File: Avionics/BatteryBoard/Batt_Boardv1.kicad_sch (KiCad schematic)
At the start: 29 parts, among them J1 Conn_02x26_Odd_Even, J2 Conn_02x26_Odd_Even, Q1 IRF7458, Q2 IRF7458

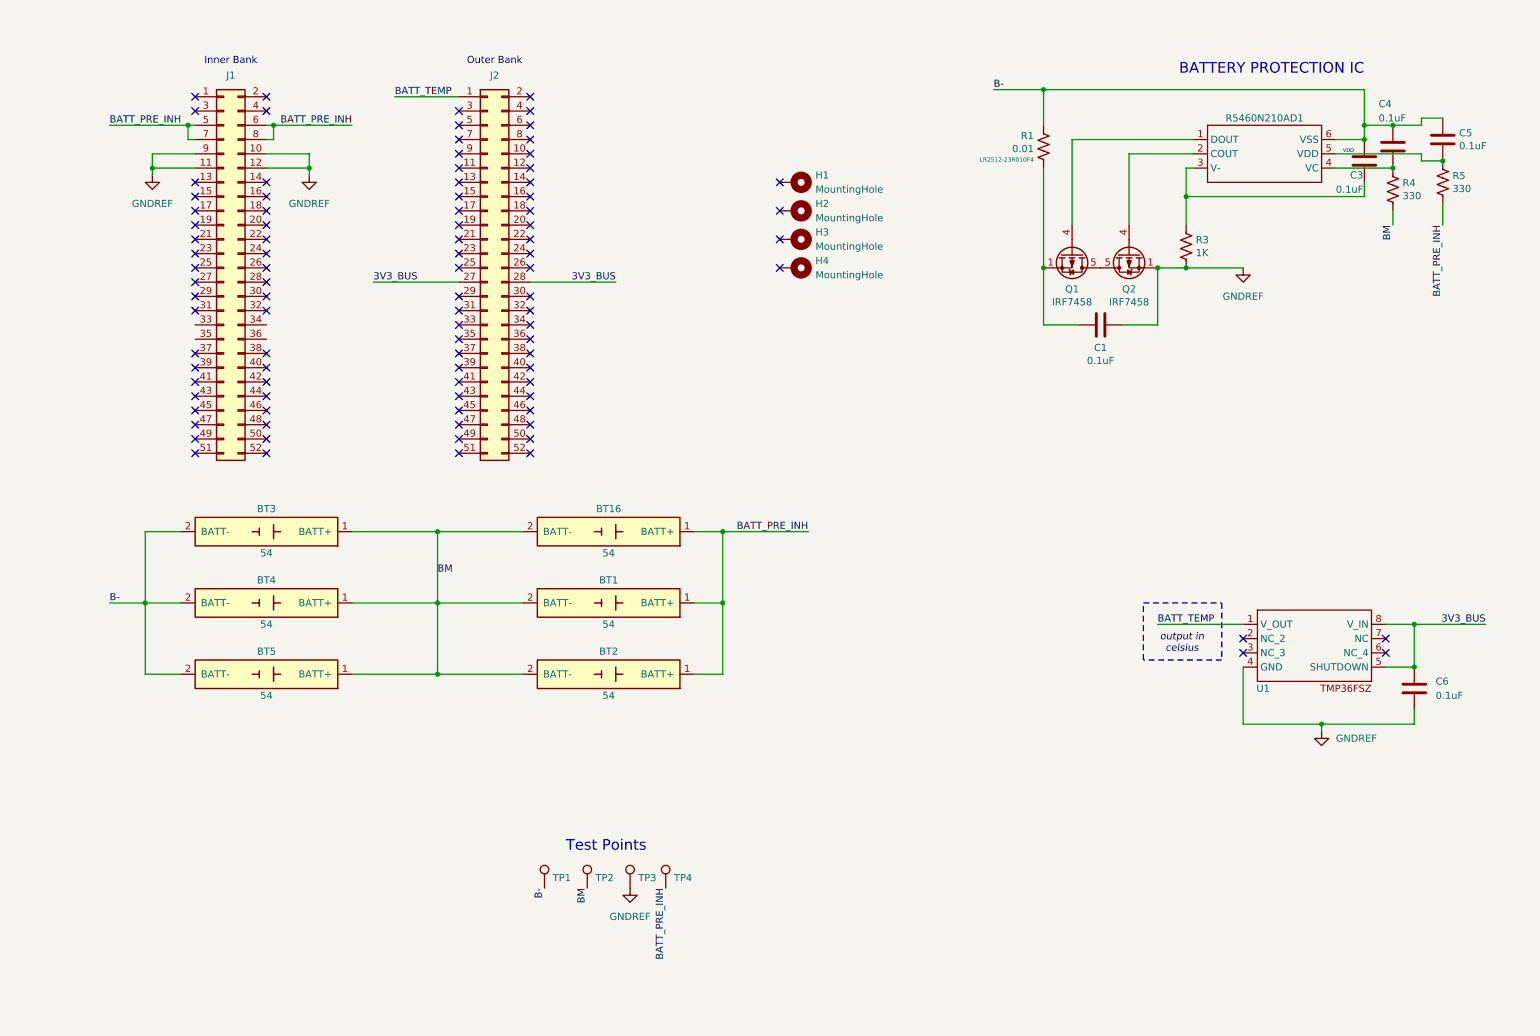
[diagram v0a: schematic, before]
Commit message: batt_brd: balance ic ref impl, renamed some stuff
* Added BQ292xx balance IC reference implementation (see datasheet)
* Changed GNDREF symbols to correct ones
* Renamed cell holders to make more sense
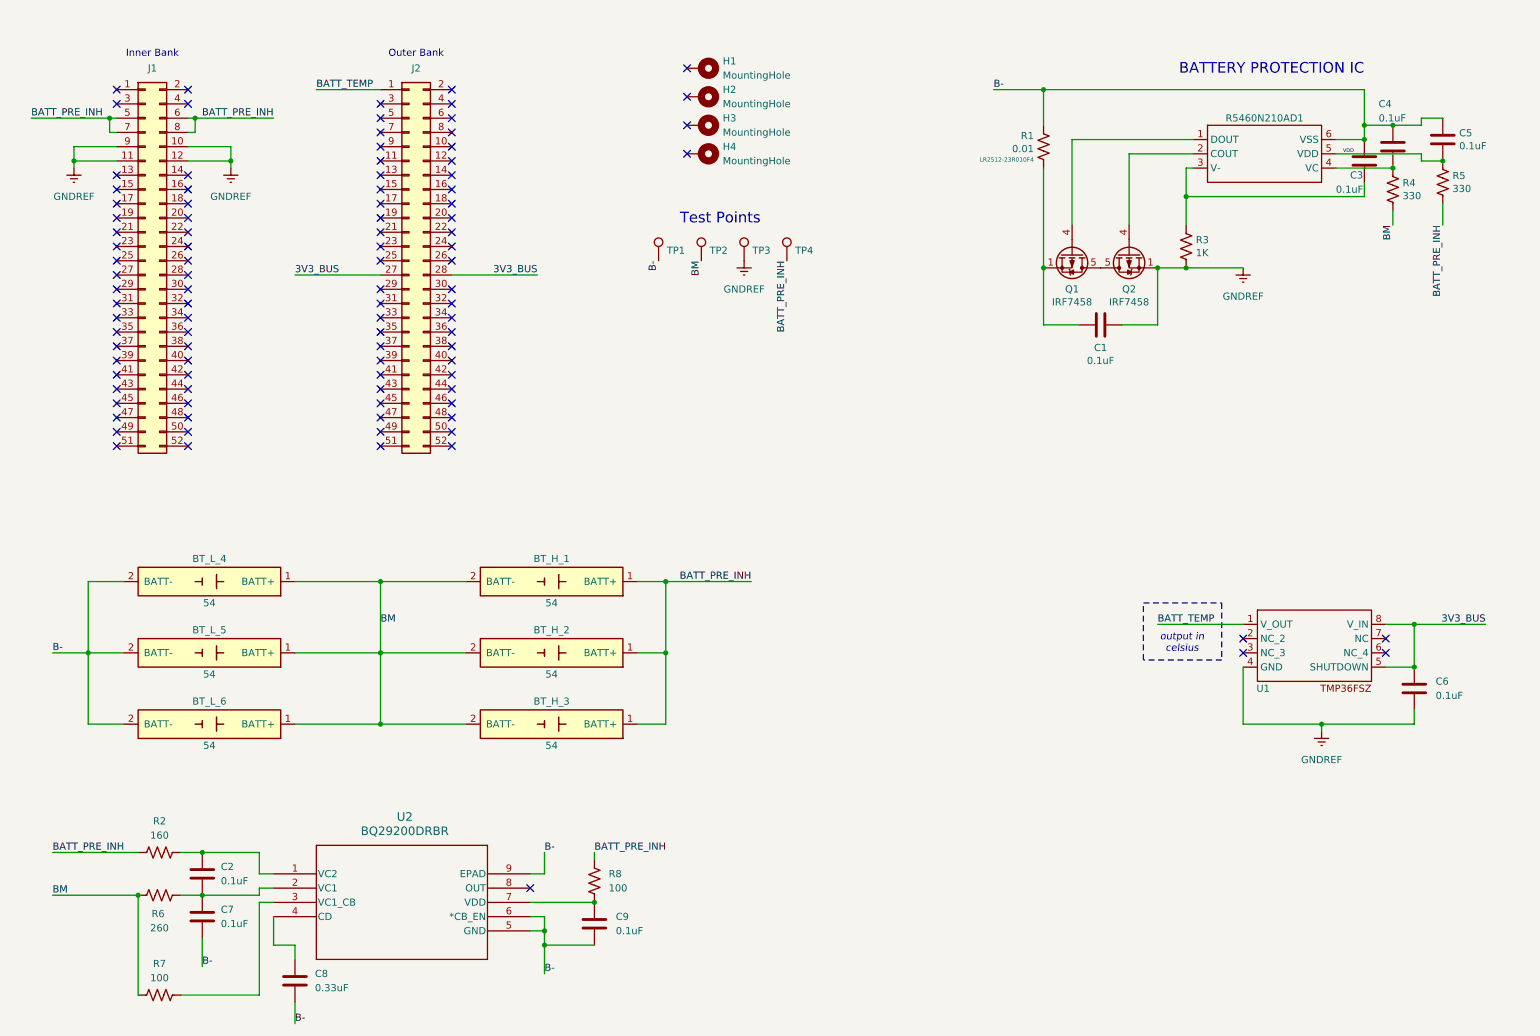
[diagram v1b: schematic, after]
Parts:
- added C2, C7, C9: 0.1uF, symbol Device:C
- added C8: 0.33uF, symbol Device:C
- added R2: 160, symbol Device:R_US
- added R6: 260, symbol Device:R_US
- added R7, R8: 100, symbol Device:R_US
- added U2: BQ29200DRBR, Package_SON:Texas_S-PVSON-N8, symbol BQ29200:BQ29200DRBR
- renumbered BT16 to BT_H_1, BT1 to BT_H_2, BT2 to BT_H_3, BT3 to BT_L_4, BT4 to BT_L_5, BT5 to BT_L_6
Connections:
- net B-: now also C7.2, C8.2, C9.2, U2.5 (GND), U2.6 (*CB_EN), U2.9 (EPAD)
- net BATT_PRE_INH: now also R2.1, R8.1
- net BM: now also R6.1, R7.1
- new net: C9.1, R8.2, U2.7 (VDD)
- new net: C2.1, R2.2, U2.1 (VC2)
- new net: C2.2, C7.1, R6.2, U2.2 (VC1)
- new net: R7.2, U2.3 (VC1_CB)
- new net: C8.1, U2.4 (CD)
- no-connect marks 97 -> 102
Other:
- moved on the sheet: BT_H_1, BT_H_2, BT_H_3, BT_L_4, BT_L_5, BT_L_6, H1, H2, H3, H4, J1, J2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

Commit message: batt_brd: reorg sch, add sub sch for heater ctrl
* Reorganized schematic
* removed temp sensor
* add sub schematic for heater control
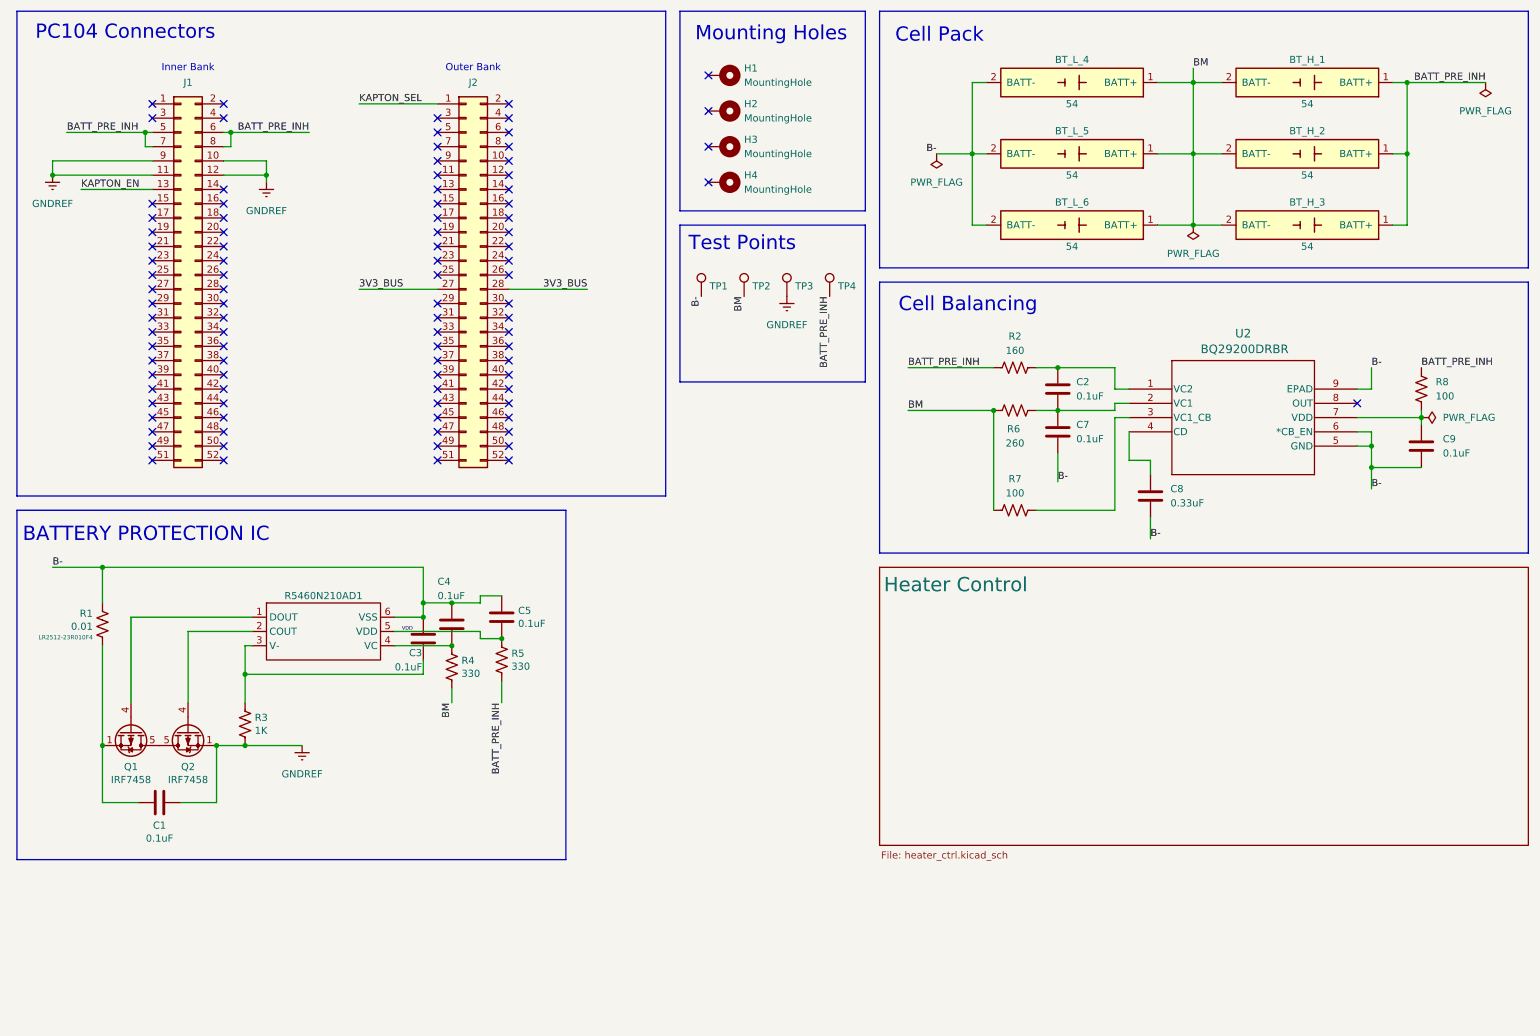
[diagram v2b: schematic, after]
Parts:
- removed C6: 0.1uF, Capacitor_SMD:C_0603_1608Metric, symbol Device:C
- removed U1: ~, Package_SO:SOIC-8_3.9x4.9mm_P1.27mm, symbol pdu:TMP36FSZ
- U2: footprint Package_SON:Texas_S-PVSON-N8 -> DRB8_1P6X2P4
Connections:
- net KAPTON_EN: now reaches J1.13 (Pin_13)
- net BATT_TEMP renamed KAPTON_SEL
- no-connect marks 102 -> 97
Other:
- added sheet Heater Control (heater_ctrl.kicad_sch)
- note added: "Cell Balancing"
- note added: "Cell Pack"
- note added: "Mounting Holes"
- note added: "PC104 Connectors"
- note removed: "output in celsius"
- company: (none) -> UChicago Space Program Avionics
- title: (none) -> Battery Carrier Board
- moved on the sheet: BT_H_1, BT_H_2, BT_H_3, BT_L_4, BT_L_5, BT_L_6, C1, C2, C3, C4, C5, C7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
